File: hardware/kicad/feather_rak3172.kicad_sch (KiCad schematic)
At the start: 51 parts, among them J1 DNP, J2 DNP, J3 USB_C_Receptacle_USB2.0, J4 SMA-KE-P903, J5 SWD, J6 JST-2PH, Q1 DMG3415UQ-7, SW1 RESET, SW2 BOOT, U1 RAK3172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

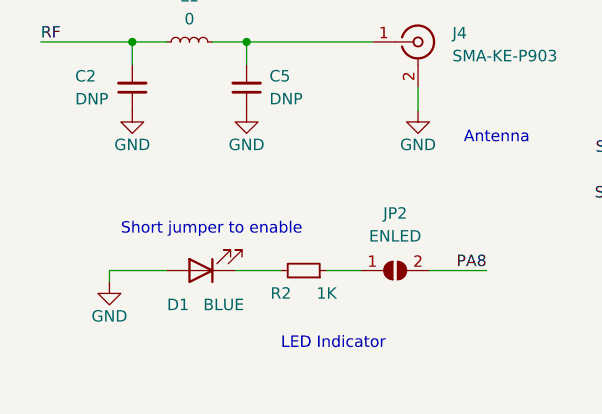
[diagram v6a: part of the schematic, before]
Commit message: fix D1 polarity
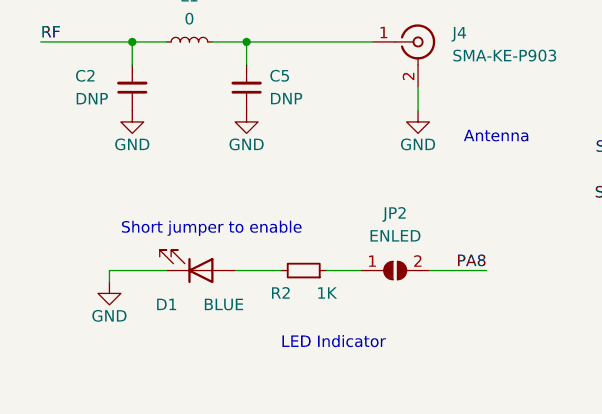
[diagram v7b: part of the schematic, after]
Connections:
- net GND: now also D1.1 (K); no longer D1.2 (A)
- net at R2.2: now also D1.2 (A); no longer D1.1 (K)
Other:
- moved on the sheet: D1
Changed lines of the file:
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@@
     (pin "1")
   )
-  (symbol (lib_id "Device:LED") (at 33.02 184.15 180) (unit 1)
+  (symbol (lib_id "Device:LED") (at 33.02 184.15 0) (mirror x) (unit 1)
     (in_bom yes) (on_board yes)
-    (property "Reference" "D1" (id 0) (at 30.48 187.96 0))
+    (property "Reference" "D1" (id 0) (at 29.21 187.96 0))
     (property "Value" "BLUE" (id 1) (at 35.56 187.96 0))
     (property "Footprint" "LED_SMD:LED_0603_1608Metric" (id 2) (at 33.02 184.15 0)
